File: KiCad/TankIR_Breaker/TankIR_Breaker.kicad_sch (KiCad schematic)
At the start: 15 parts, among them J1 VBATT, J2 TRIGGER, J3 SERVO, J4 RC, J5 APPLE, J6 SOUND, J7 IR_OUT, J8 MUZZLE, Q1 BC337, Q2 BC337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

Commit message: Update TankIR_Breaker.kicad_sch
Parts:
- R1, R2: footprint Resistor_SMD:R_0805_2012Metric_Pad1.20x1.40mm_HandSolder -> Resistor_THT:R_Axial_DIN0204_L3.6mm_D1.6mm_P2.54mm_Vertical
- R3: footprint Resistor_SMD:R_1210_3225Metric_Pad1.30x2.65mm_HandSolder -> Resistor_THT:R_Axial_DIN0204_L3.6mm_D1.6mm_P2.54mm_Vertical
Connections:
- net +BATT: now also J1.1 (Pin_1); no longer J1.2 (Pin_2)
- net GND: now also J1.2 (Pin_2); no longer J1.1 (Pin_1)
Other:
- moved on the sheet: J1
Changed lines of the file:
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@@
 			)
 		)
-		(property "Footprint" "Resistor_SMD:R_0805_2012Metric_Pad1.20x1.40mm_HandSolder"
+		(property "Footprint" "Resistor_THT:R_Axial_DIN0204_L3.6mm_D1.6mm_P2.54mm_Vertical"
 			(at 214.63 75.438 90)
 			(effects
@@
 			)
 		)
-		(property "Footprint" "Resistor_SMD:R_0805_2012Metric_Pad1.20x1.40mm_HandSolder"
+		(property "Footprint" "Resistor_THT:R_Axial_DIN0204_L3.6mm_D1.6mm_P2.54mm_Vertical"
 			(at 214.63 98.298 90)
 			(effects
@@
 			)
 		)
-		(property "Footprint" "Resistor_SMD:R_1210_3225Metric_Pad1.30x2.65mm_HandSolder"
+		(property "Footprint" "Resistor_THT:R_Axial_DIN0204_L3.6mm_D1.6mm_P2.54mm_Vertical"
 			(at 231.14 66.548 90)
 			(effects
@@
 	(symbol
 		(lib_id "Connector_Generic:Conn_01x02")
-		(at 25.4 91.44 180)
-		(unit 1)
-		(exclude_from_sim no)
-		(in_bom yes)
-		(on_board yes)
-		(dnp no)
-		(fields_autoplaced yes)
+		(at 25.4 88.9 0)
+		(mirror y)
+		(unit 1)
+		(exclude_from_sim no)
+		(in_bom yes)
+		(on_board yes)
+		(dnp no)
 		(property "Reference" "J1"
-			(at 25.4 82.55 0)
+			(at 22.606 89.916 0)
 			(effects
 				(font
@@
 		)
 		(property "Value" "VBATT"
-			(at 25.4 85.09 0)
+			(at 25.908 86.106 0)
 			(effects
 				(font
@@
 		)
 		(property "Footprint" "Connector_JST:JST_PH_B2B-PH-K_1x02_P2.00mm_Vertical"
-			(at 25.4 91.44 0)
+			(at 25.4 88.9 0)
 			(effects
 				(font
@@
 		)
 		(property "Datasheet" "~"
-			(at 25.4 91.44 0)
+			(at 25.4 88.9 0)
 			(effects
 				(font
@@
 		)
 		(property "Description" "Generic connector, single row, 01x02, script generated (kicad-library-utils/schlib/autogen/connector/)"
-			(at 25.4 91.44 0)
+			(at 25.4 88.9 0)
 			(effects
 				(font
@@
 		(on_board yes)
 		(dnp no)
-		(fields_autoplaced yes)
 		(property "Reference" "J2"
-			(at 25.4 95.25 0)
+			(at 24.13 99.06 0)
 			(effects
 				(font
@@
 		)
 		(property "Value" "TRIGGER"
-			(at 25.4 97.79 0)
-			(effects
-				(font
+			(at 18.796 99.314 0)
+			(effects
+				(font

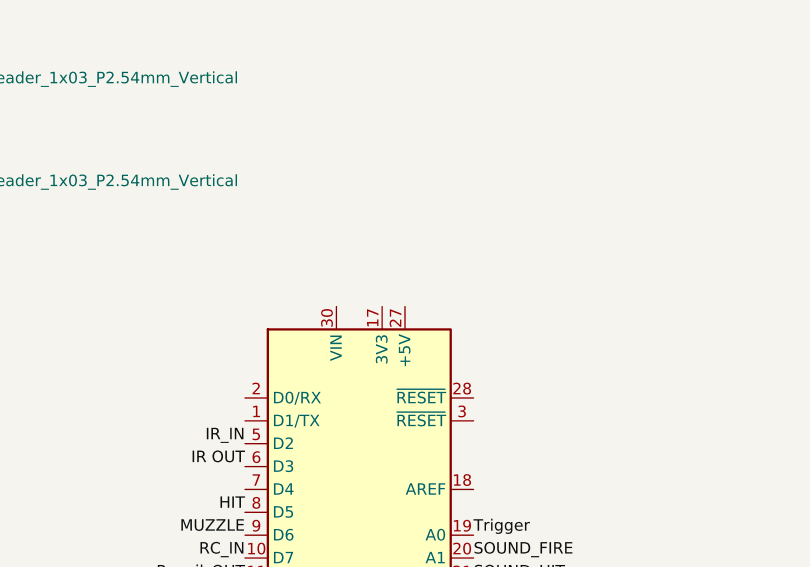
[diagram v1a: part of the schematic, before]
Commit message: fix
Fixed missing 5V connection
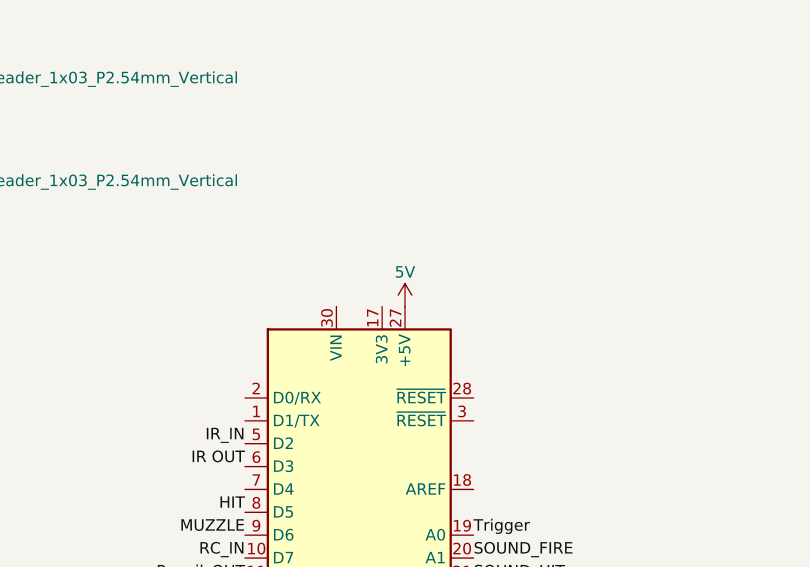
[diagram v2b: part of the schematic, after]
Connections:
- net 5V: now also A1.27 (+5V)
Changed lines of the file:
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@@
+	)
+	(symbol
+		(lib_id "SparkFun-PowerSymbol:5V")
+		(at 149.86 73.66 0)
+		(unit 1)
+		(exclude_from_sim no)
+		(in_bom yes)
+		(on_board yes)
+		(dnp no)
+		(fields_autoplaced yes)
+		(property "Reference" "#PWR08"
+			(at 149.86 77.47 0)
+			(effects
+				(font
+					(size 1.27 1.27)
+				)
+				(hide yes)
+			)
+		)
+		(property "Value" "5V"
+			(at 149.86 69.85 0)
+			(do_not_autoplace yes)
+			(effects
+				(font
+					(size 1.27 1.27)
+				)
+			)
+		)
+		(property "Footprint" ""
+			(at 149.86 73.66 0)
+			(effects
+				(font
+					(size 1.27 1.27)
+				)
+				(hide yes)
+			)
+		)
+		(property "Datasheet" ""
+			(at 149.86 73.66 0)
+			(effects
+				(font
+					(size 1.27 1.27)
+				)
+				(hide yes)
+			)
+		)
+		(property "Description" "Power symbol creates a global label with name \"5V\""
+			(at 149.86 73.66 0)
+			(effects
+				(font
+					(size 1.27 1.27)
+				)
+				(hide yes)
+			)
+		)
+		(pin "1"
+		)
+		(instances
+			(project "TankIR_Breaker"
+				(path "/09972bc1-aadf-4a5a-b293-70d074730d27"
+					(reference "#PWR08")
+					(unit 1)
+				)
+			)
+		)
 	)
 	(symbol

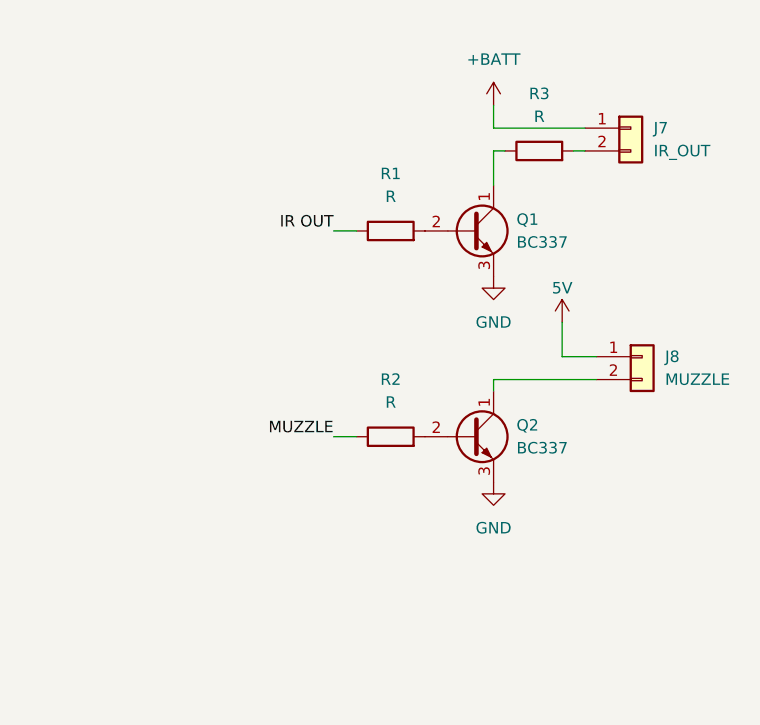
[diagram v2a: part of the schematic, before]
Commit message: REV2
Modified board for more reliable fabrication and added Pull-down resistors to avoid Transistor current leakage
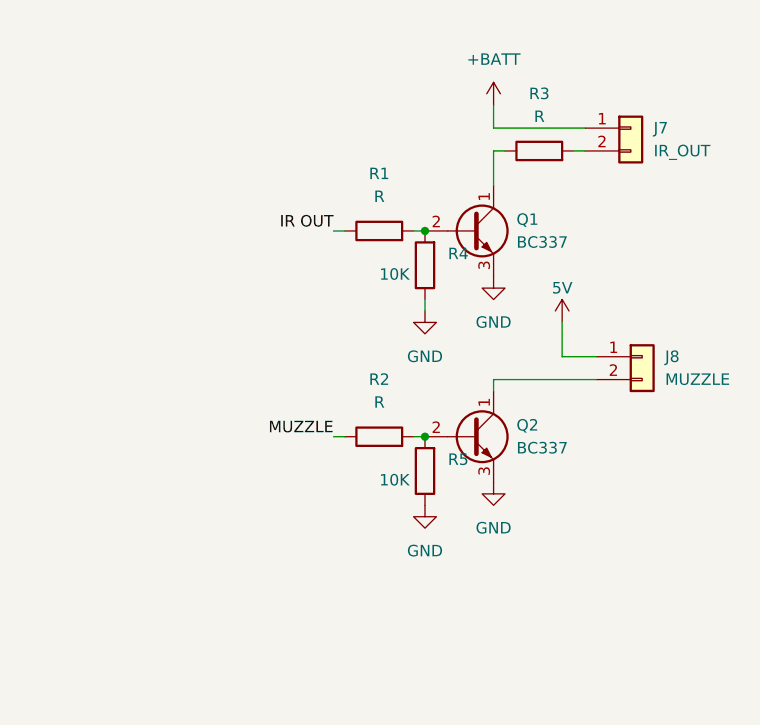
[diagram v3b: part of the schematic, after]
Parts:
- added R4, R5: 10K, Resistor_THT:R_Axial_DIN0204_L3.6mm_D1.6mm_P2.54mm_Vertical, symbol Device:R
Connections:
- net GND: now also R4.1, R5.1
- net at Q1.2 (B), R1.2: now also R4.2
- net at Q2.2 (B), R2.2: now also R5.2
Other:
- moved on the sheet: R1, R2

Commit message: Correction
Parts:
- R1, R2: value R -> 200
- R3: value R -> 3.3
- R4, R5: value 10K -> 2.2k
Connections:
- net IR OUT: now also R4.2
- net MUZZLE: now also R5.2
- net at Q1.2 (B), R1.2: no longer R4.2
- net at Q2.2 (B), R2.2: no longer R5.2
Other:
- moved on the sheet: A1, J1, J2, J3, J4, J5, J6, J7, J8, Q1, Q2, R1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
